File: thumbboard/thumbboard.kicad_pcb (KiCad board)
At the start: 2 copper layers, 82 x 49 mm, 11 parts, among them J1 Conn_01x05_MountingPin, SW1 SW_Push, SW2 SW_Push, SW3 SW_Push, SW4 SW_Push, T3 Tab, T4 Tab, T5 Tab, T6 Tab

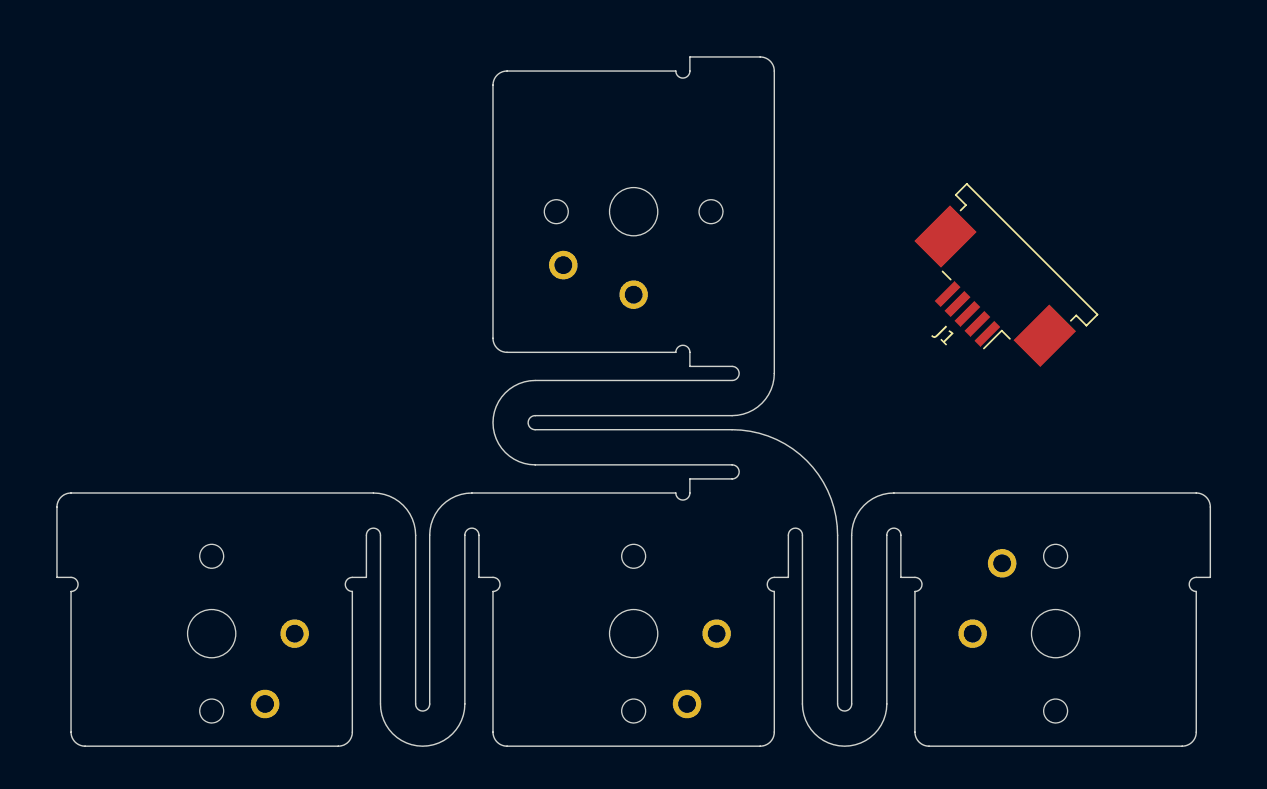
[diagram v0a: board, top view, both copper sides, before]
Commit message: complete thumbboard; increase arclength and sharpen angle
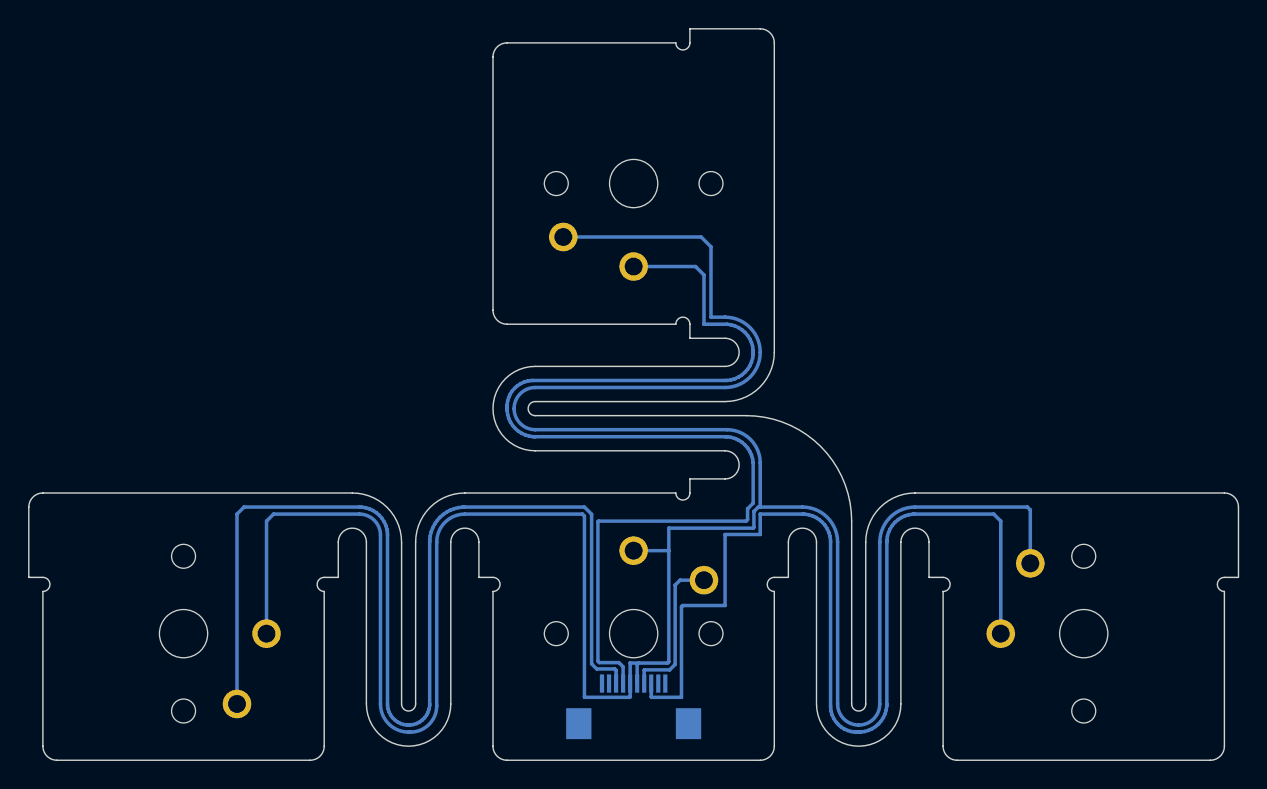
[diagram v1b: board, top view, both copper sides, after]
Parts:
- removed T5, T6: Tab, PCM_kikit:Tab
- added T4: Tab, PCM_kikit:Tab, F.Cu at (190.8, 103.0)
- added T4: Tab, PCM_kikit:Tab, F.Cu at (154.0, 66.2)
- J1: footprint Connector_FFC-FPC:TE_84952-5_1x05-1MP_P1.0mm_Horizontal -> Custom:FFC_Clamshell_0.5mm_1x10; moved to B.Cu
- moved J1 38.3 mm to (147.5, 114.5), turned to 180 degrees
- moved T4 8.94 mm to (104.2, 103.0)
- moved T1 4.47 mm to (115.5, 118.8)
- moved T2 4.47 mm to (179.5, 118.8)
- moved T3 4.00 mm to (147.5, 118.8)
- moved SW1 2.00 mm to (179.5, 109.5)
- moved SW3 2.00 mm to (147.5, 77.5)
- moved SW4 2.00 mm to (115.5, 109.5)
- turned SW2 to 180 degrees
- renumbered T4 to T1, T4 to T2, T5 to T4
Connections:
- J1 pad 1: ROW_A -> unconnected-(J1-Pin_1-Pad1)
- J1 pad 2: ROW_B -> unconnected-(J1-Pin_2-Pad2)
- J1 pad 3: COL -> ROW_A
- J1 pad 4: ROW_C -> ROW_B
- J1 pad 5: ROW_D -> COL
- SW1 pad 1: COL -> ROW_A
- SW1 pad 2: ROW_A -> COL
- SW3 pad 1: COL -> ROW_C
- SW3 pad 2: ROW_C -> COL
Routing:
- net COL: track 0.00 -> 214.3 mm
- net ROW_C: track 0.00 -> 80.9 mm
- net ROW_D: track 0.00 -> 80.4 mm
- net ROW_A: track 0.00 -> 74.6 mm
- net ROW_B: track 0.00 -> 11.2 mm
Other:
- board size 82 x 49 mm -> 86 x 52 mm

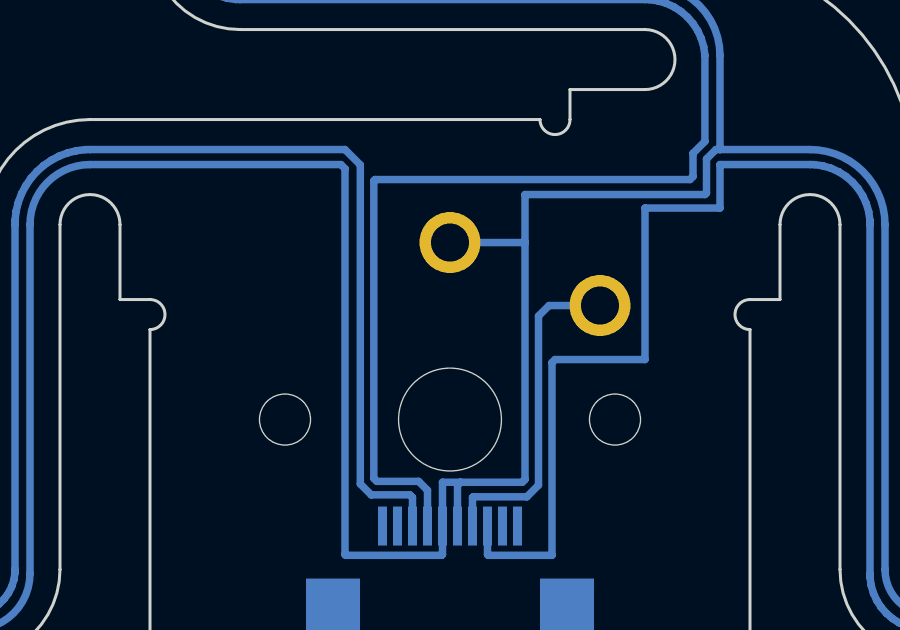
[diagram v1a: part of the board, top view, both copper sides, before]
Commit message: Add label to thumbboard; make bottom tabs narrower (hard to break off the frame without damaging the thing)
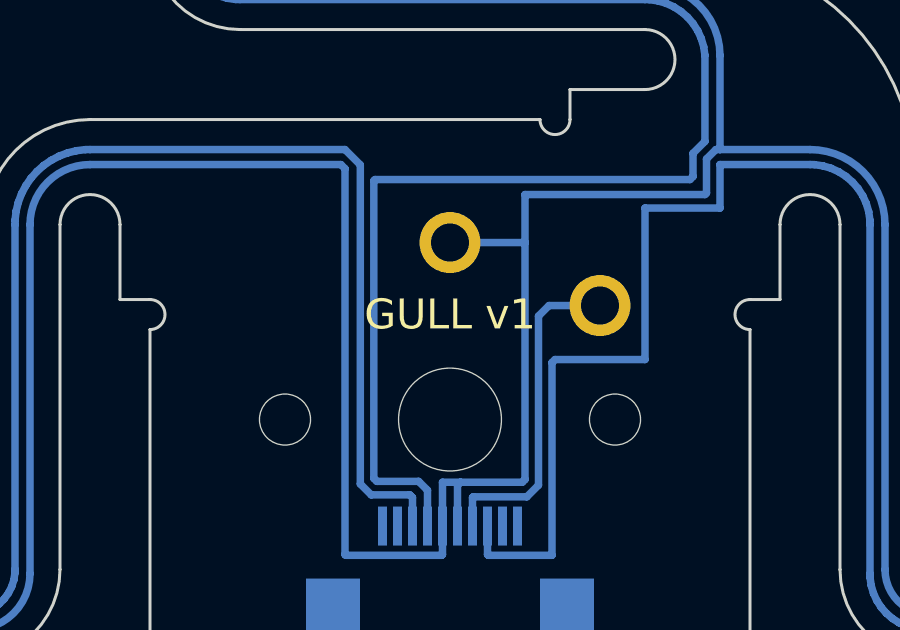
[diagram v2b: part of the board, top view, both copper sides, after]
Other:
- board text added: "GULL v1"
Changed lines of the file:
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@@
         (effects (font (size 1.2 1.2) (thickness 0.2)))
     )
-    (fp_text user "KIKIT: width: 15mm" (at -5.5 0) (layer "Dwgs.User")
+    (fp_text user "KIKIT: width: 10mm" (at -5.5 0) (layer "Dwgs.User")
         (effects (font (size 1 1) (thickness 0.15)))
     )
@@
         (effects (font (size 1.2 1.2) (thickness 0.2)))
     )
-    (fp_text user "KIKIT: width: 15mm" (at -5.5 0) (layer "Dwgs.User")
+    (fp_text user "KIKIT: width: 10mm" (at -5.5 0) (layer "Dwgs.User")
         (effects (font (size 1 1) (thickness 0.15)))
     )
@@
         (effects (font (size 1.2 1.2) (thickness 0.2)))
     )
-    (fp_text user "KIKIT: width: 15mm" (at -5.5 0) (layer "Dwgs.User")
+    (fp_text user "KIKIT: width: 10mm" (at -5.5 0) (layer "Dwgs.User")
         (effects (font (size 1 1) (thickness 0.15)))
     )
@@
   (gr_arc (start 166.5 114.5) (mid 163.5 117.5) (end 160.5 114.5)
     (stroke (width 0.1) (type default)) (layer "Edge.Cuts"))
+  (gr_text "GULL v1" (at 147.5 106) (layer "F.SilkS")
+    (effects (font (size 1 1) (thickness 0.15)))
+  )
   (dimension (type orthogonal) (layer "Cmts.User")
     (pts (xy 137.5 114.5) (xy 134.5 114.5))

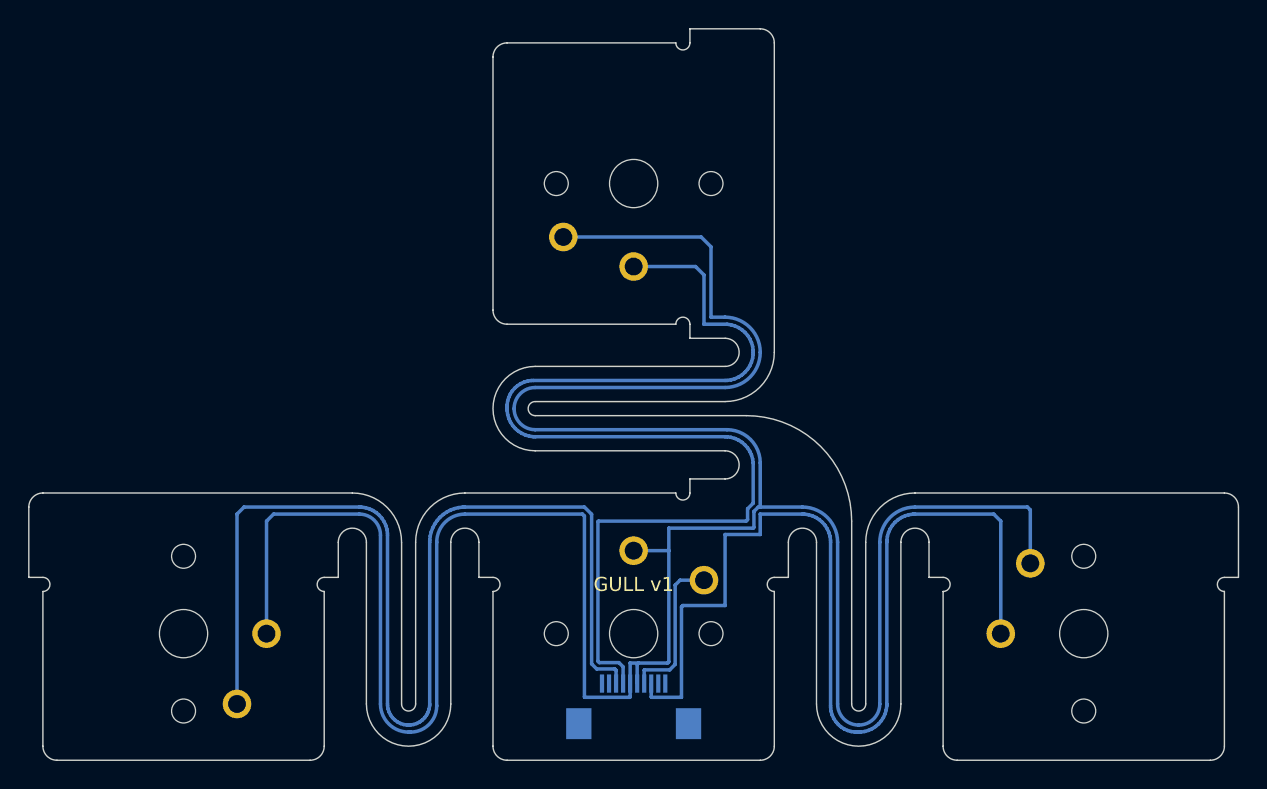
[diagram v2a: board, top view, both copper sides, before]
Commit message: Make thumbboard reversible; move connector
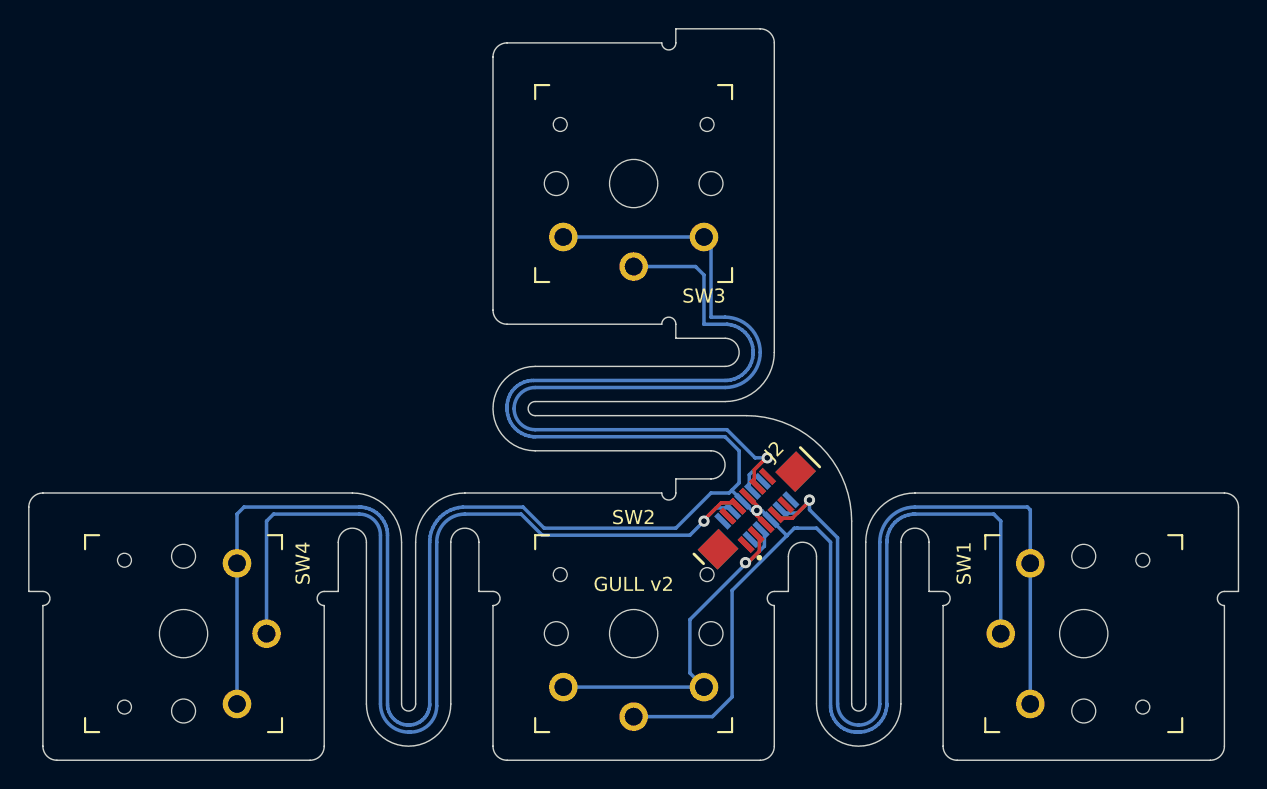
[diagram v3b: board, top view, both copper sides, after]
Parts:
- added J2: Conn_01x05_MountingPin, Custom:GCT_FFC2A33-10-T-R_REVA_Clipped2, F.Cu at (156.3, 100.7)
- J1: footprint Custom:FFC_Clamshell_0.5mm_1x10 -> Custom:GCT_FFC2A33-10-T-R_REVA_Clipped1
- SW1, SW3, SW4: footprint keyswitches:SW_PG1350 -> keyswitches:SW_PG1350_reversible
- SW2: footprint keyswitches:SW_PG1350 -> keyswitches:SW_PG1350_reversible_MissingCorner
- moved J1 16.3 mm to (156.3, 100.7), turned to -135 degrees
- moved T4 0.50 mm to (190.8, 103.5)
- moved T4 0.50 mm to (104.2, 103.5)
- moved T4 0.50 mm to (153.5, 66.2)
- turned SW2 to 0 degrees
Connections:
- SW1 pad 1: ROW_A -> COL
- SW1 pad 2: COL -> ROW_A
- SW2 pad 2: ROW_B -> ROW_C
- SW3 pad 1: ROW_C -> COL
- SW3 pad 2: COL -> ROW_B
- SW4 pad 1: COL -> ROW_D
- SW4 pad 2: ROW_D -> COL
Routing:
- net ROW_B: track 11.2 -> 65.5 mm, vias 0 -> 1
- net ROW_C: track 80.9 -> 26.6 mm, vias 0 -> 1
- net ROW_A: track 74.6 -> 62.9 mm, vias 0 -> 1
- net ROW_D: track 80.4 -> 73.5 mm, vias 0 -> 1
- net COL: track 214.3 -> 211.7 mm, vias 0 -> 1
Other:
- outline, holes or cut-outs redrawn
- board text added: "GULL v2"
- board text removed: "GULL v1"
